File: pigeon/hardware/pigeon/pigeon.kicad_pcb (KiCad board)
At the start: 2 copper layers, 120 x 30 mm, 16 parts, among them J1 Battery, SW1 Power Switch, U1 ESP32-S3-Zero, U2 Adafruit_Ultimate_GPS, U3 Adafruit_RFM95W

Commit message: pigeon: version 1 of pcb
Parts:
- moved J1 2.12 mm to (98.0, 94.8)
- moved C1 0.63 mm to (101.6, 86.4)
- moved R1 0.63 mm to (101.6, 83.8)
- moved BZ1 0.31 mm to (117.3, 95.5)
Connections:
- U1 pad 5: /GPS_PPS -> /GPS_RX
- U1 pad 6: /GPS_RX -> /GPS_TX
- U1 pad 7: /GPS_TX -> /GPS_FIX
- U1 pad 8: /GPS_FIX -> /GPS_PPS
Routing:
- net /GPS_PPS: track 37.8 -> 48.0 mm
- net Net-(J1-Pin_1): track 17.6 -> 20.5 mm
- net /GPS_RX: track 30.0 -> 29.0 mm
- net /GPS_FIX: track 30.0 -> 29.0 mm
- net /GPS_TX: track 30.0 -> 29.0 mm
- net Net-(C1-Pad2): track 2.41 -> 3.04 mm
- net /VBAT: track 33.3 -> 34.0 mm
- net /VBAT_SENSE: track 20.0 -> 19.3 mm
- net GND: vias 0 -> 13
- added copper zone on B.Cu, net GND
- added copper zone on F.Cu, net GND
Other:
- board text added: "AVES Pigeon"
- board text added: "Designed by Adam Brandt"
- board text added: "GND"
- board text added: "OFF"
- board text added: "ON"
- board text added: "VBAT"
- board text added: "Version 1.0 2026-08"

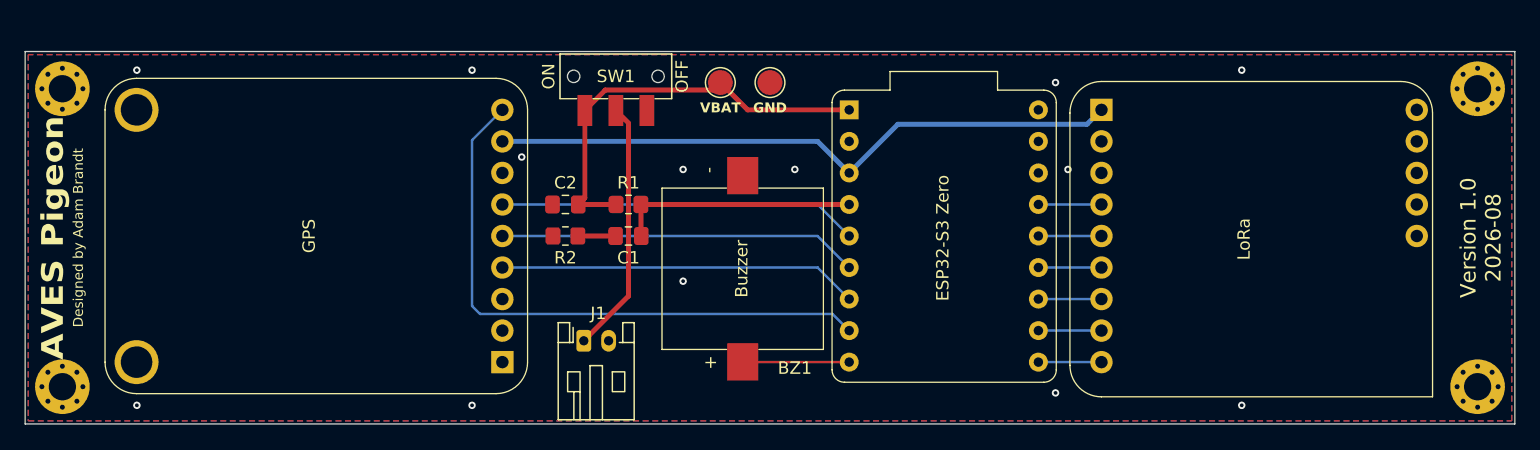
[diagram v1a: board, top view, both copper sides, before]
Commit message: pigeon: updated pcb to include mode switch
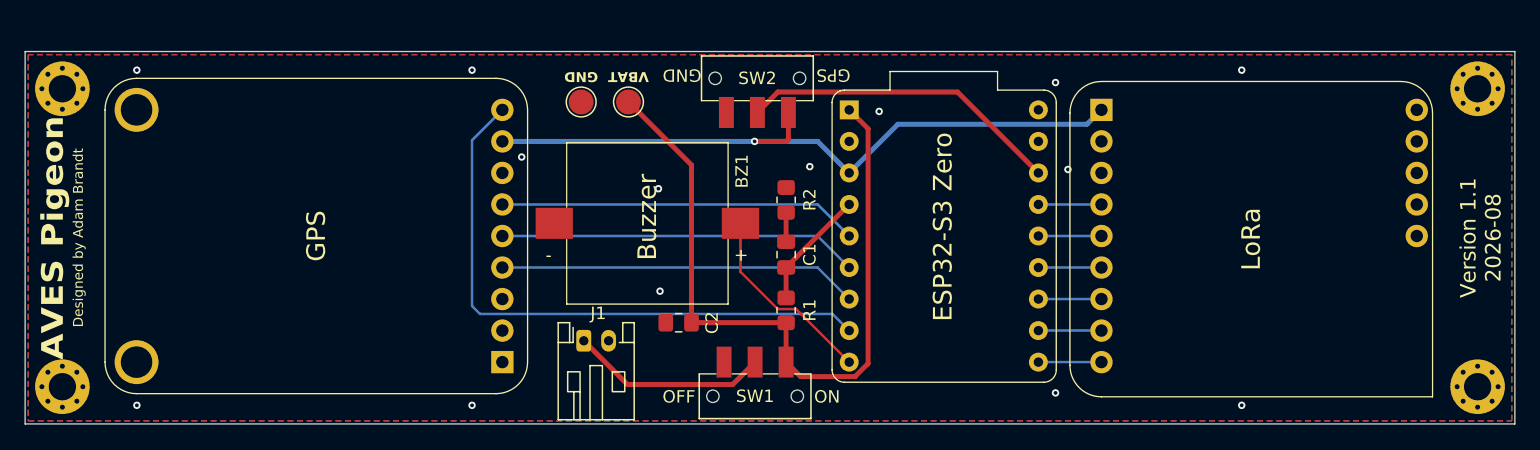
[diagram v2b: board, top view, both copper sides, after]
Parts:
- added SW2: Mode Switch, AVES:SW_CK_JS102011SAQN, F.Cu at (112.0, 73.7)
- moved SW1 28.1 mm to (111.8, 99.3), turned to 0 degrees
- moved BZ1 18.3 mm to (109.6, 78.8), turned to 180 degrees
- moved R2 18.0 mm to (114.3, 83.5), turned to 90 degrees
- moved R1 15.3 mm to (114.3, 92.3), turned to 90 degrees
- moved TP2 15.3 mm to (97.8, 75.6), turned to 0 degrees
- moved C2 13.2 mm to (105.6, 93.3)
- moved C1 12.8 mm to (114.3, 87.9), turned to 90 degrees
- moved TP1 7.56 mm to (101.6, 75.6), turned to 0 degrees
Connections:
- U1 pad 16: unconnected-(U1-GPIO13-Pad16) -> /MODE_SW
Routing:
- net /MODE_SW: track 0.00 -> 26.0 mm
- net /VBAT: track 34.0 -> 59.3 mm
- net /VBAT_SENSE: track 19.3 -> 9.63 mm
- net /BUZZER: track 8.59 -> 15.7 mm
- net +3V3: track 51.4 -> 56.4 mm, vias 0 -> 1
- net Net-(J1-Pin_1): track 20.5 -> 16.0 mm
- net Net-(C1-Pad2): track 3.04 -> 2.37 mm
- net GND: vias 13 -> 14
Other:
- board text added: "GPS"
- board text added: "Version 1.1 2026-08"
- board text removed: "Version 1.0 2026-08"

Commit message: added rounded corners to pigeon pcb
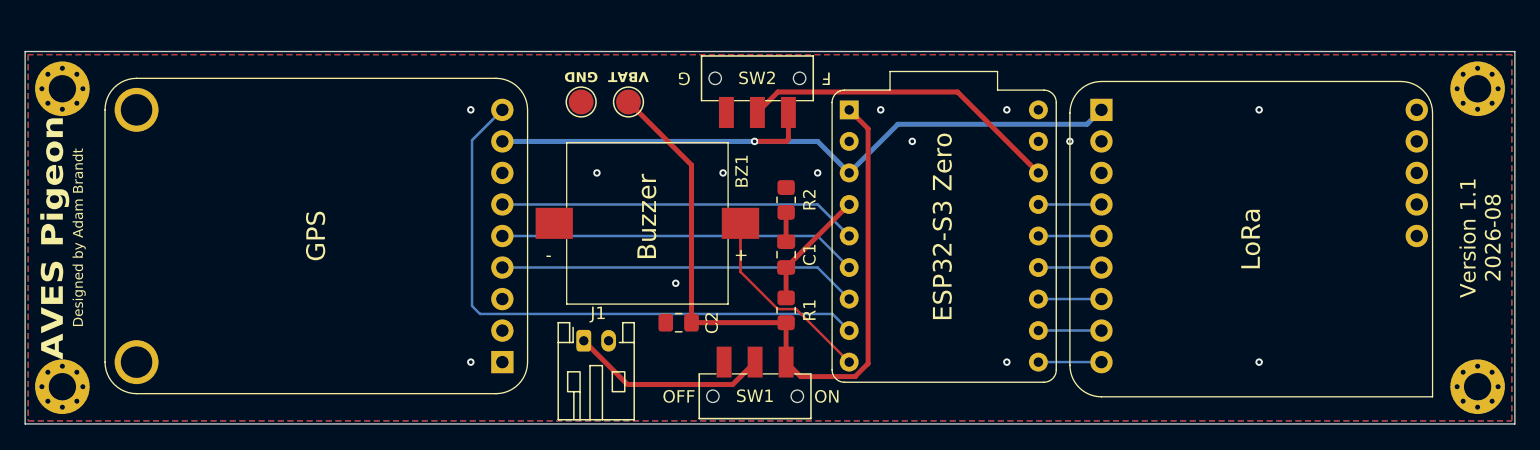
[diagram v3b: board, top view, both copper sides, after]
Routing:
- net GND: vias 14 -> 13
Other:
- board text added: "F"
- board text added: "G"
- board text removed: "GPS"
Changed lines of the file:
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@@
 		(start 53 71.5)
 		(end 173 101.5)
+		(radius 3)
 		(stroke
 			(width 0.05)
@@
 		)
 	)
-	(gr_text "GND"
-		(at 105.918 73.406 180)
+	(gr_text "G"
+		(at 106.085 73.66 180)
 		(layer "F.SilkS")
 		(effects
@@
 		)
 	)
-	(gr_text "GPS"
-		(at 118.11 73.406 180)
+	(gr_text "F"
+		(at 117.5512 73.66 180)
 		(layer "F.SilkS")
 		(effects
@@
 	)
 	(via
-		(at 93 80)
+		(at 99.06 81.28)
 		(size 0.6)
 		(drill 0.3)
@@
 	)
 	(via
-		(at 137 81)
+		(at 137.16 78.74)
 		(size 0.6)
 		(drill 0.3)
@@
 	)
 	(via
-		(at 136 74)
+		(at 132.08 76.2)
 		(size 0.6)
 		(drill 0.3)
@@
 	)
 	(via
-		(at 151 73)
+		(at 152.4 76.2)
 		(size 0.6)
 		(drill 0.3)
@@
 	)
 	(via
-		(at 121.793 76.327)
+		(at 121.92 76.2)
 		(size 0.6)
 		(drill 0.3)
@@
 	)
 	(via
-		(at 104.013 82.55)
+		(at 109.22 81.28)
 		(size 0.6)
 		(drill 0.3)
@@
 	)
 	(via
-		(at 62 100)
+		(at 88.9 96.52)
 		(size 0.6)
 		(drill 0.3)
@@
 	)
 	(via
-		(at 89 100)
+		(at 152.4 96.52)
 		(size 0.6)
 		(drill 0.3)
@@
 	)
 	(via
-		(at 151 100)
+		(at 116.84 81.28)
 		(size 0.6)
 		(drill 0.3)
@@
 	)
 	(via
-		(at 62 73)
+		(at 105.41 90.17)
 		(size 0.6)
 		(drill 0.3)
@@
 	)
 	(via
-		(at 116.205 80.772)
+		(at 88.9 76.2)
 		(size 0.6)
 		(drill 0.3)
@@
 	)
 	(via
-		(at 104.14 90.805)
+		(at 124.46 78.74)
 		(size 0.6)
 		(drill 0.3)
@@
 	)
 	(via
-		(at 89 73)
-		(size 0.6)
-		(drill 0.3)
-		(layers "F.Cu" "B.Cu")
-		(free yes)
-		(net "GND")
-	)
-	(via
-		(at 136 99)
+		(at 132.08 96.52)
 		(size 0.6)
 		(drill 0.3)
@@
 	)
 	(segment
+		(start 111.985 76.41)
+		(end 113.635 74.76)
+		(width 0.4)
+		(layer "F.Cu")
+		(net "/MODE_SW")
+	)
+	(segment
+		(start 113.635 74.76)
+		(end 128.1 74.76)
+		(width 0.4)
+		(layer "F.Cu")
+		(net "/MODE_SW")
+	)
+	(segment
+		(start 128.1 74.76)
+		(end 134.62 81.28)
+		(width 0.4)
+		(layer "F.Cu")
+		(net "/MODE_SW")
+	)
+	(segment
 		(start 134.62 96.52)
 		(end 139.7 96.52)
@@
 		(layer "B.Cu")
 		(net "/LORA_DIO0")
-	)
-	(segment
-		(start 111.985 76.41)
-		(end 113.635 74.76)
-		(width 0.4)
-		(layer "F.Cu")
-		(net "/MODE_SW")
-	)
-	(segment
-		(start 113.635 74.76)
-		(end 128.1 74.76)
-		(width 0.4)
-		(layer "F.Cu")
-		(net "/MODE_SW")
-	)
-	(segment
-		(start 128.1 74.76)
-		(end 134.62 81.28)
-		(width 0.4)
-		(layer "F.Cu")
-		(net "/MODE_SW")
 	)
 	(zone
@@
 		(polygon
 			(pts
-				(xy 120.75 92.25) (xy 132 92.25) (xy 132 98.25) (xy 120.75 98.25)
-			)
-		)
+				(xy 120.75 92.25) (xy 130.81 92.25) (xy 130.81 98.25) (xy 120.75 98.25)
+			)
+		)

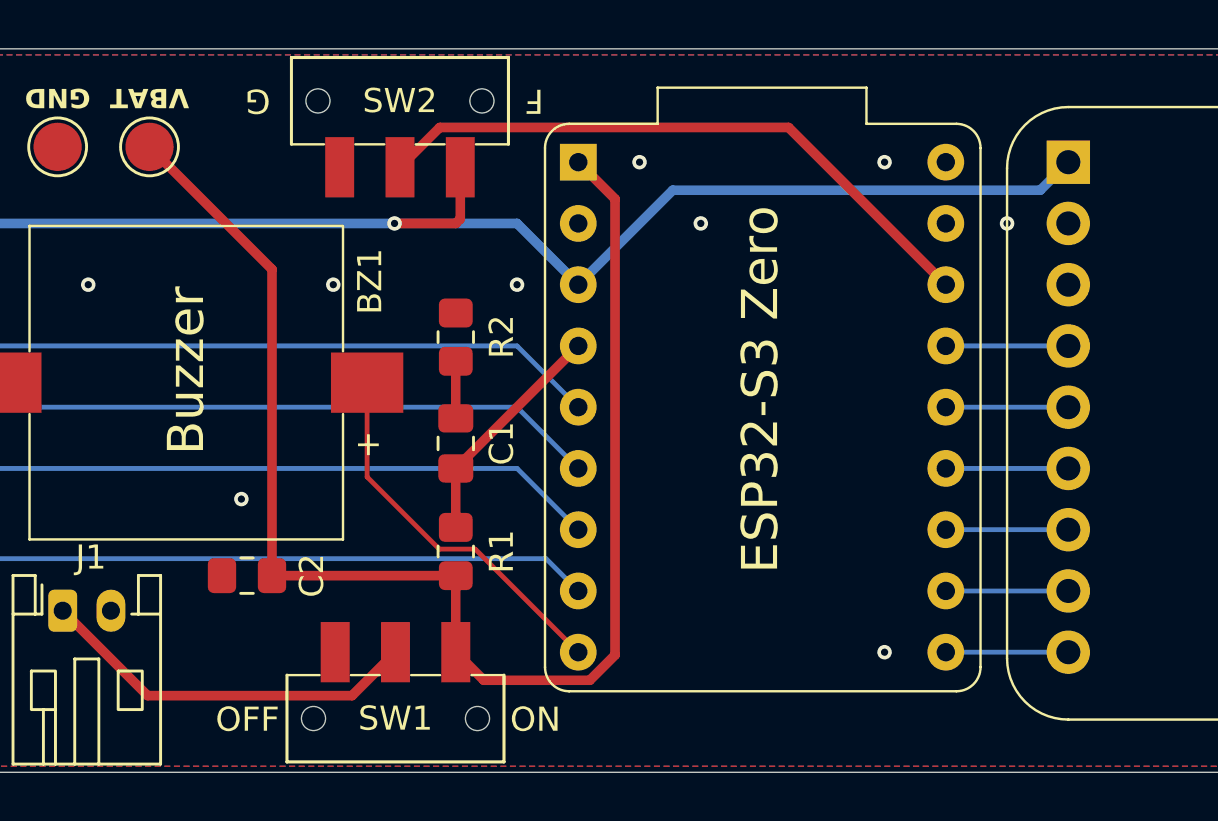
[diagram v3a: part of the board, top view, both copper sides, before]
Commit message: pigeon: completed version 1.1 of carrier pcb. - Added rounded corners - Changed C1 to be parralel with R2 - Added mode swtich
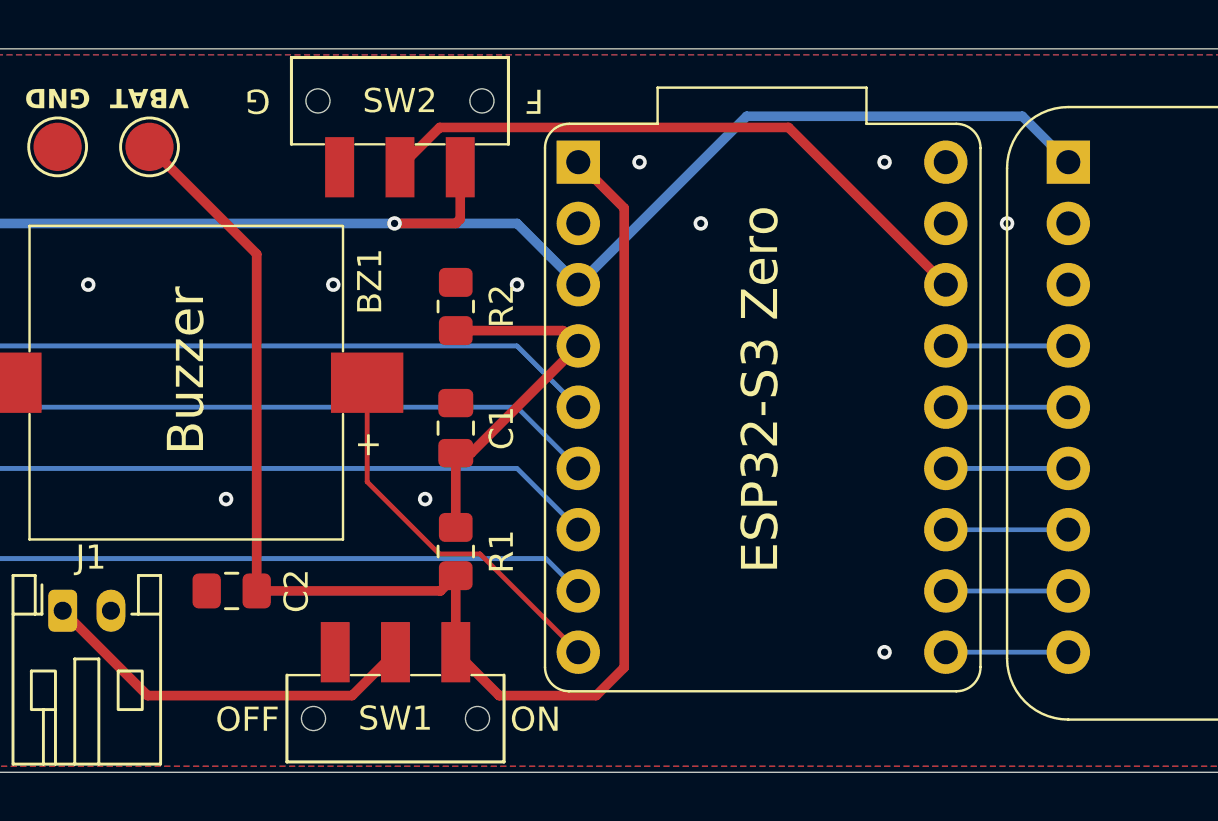
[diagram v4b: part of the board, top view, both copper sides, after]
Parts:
- moved R2 1.27 mm to (114.3, 82.2)
- moved C2 0.90 mm to (105.0, 94.0)
- moved C1 0.63 mm to (114.3, 87.2)
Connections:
- C1 pad 2: Net-(C1-Pad2) -> GND
- R2 pad 1: Net-(C1-Pad2) -> /VBAT_SENSE
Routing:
- net /VBAT_SENSE: track 9.63 -> 15.3 mm
- net /VBAT: track 59.3 -> 61.9 mm
- net Net-(C1-Pad2): track 2.37 -> 0.00 mm
- net +3V3: track 56.4 -> 57.9 mm
- net GND: vias 13 -> 14
